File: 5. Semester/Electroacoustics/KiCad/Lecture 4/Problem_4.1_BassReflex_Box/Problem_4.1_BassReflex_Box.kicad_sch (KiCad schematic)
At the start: 14 parts

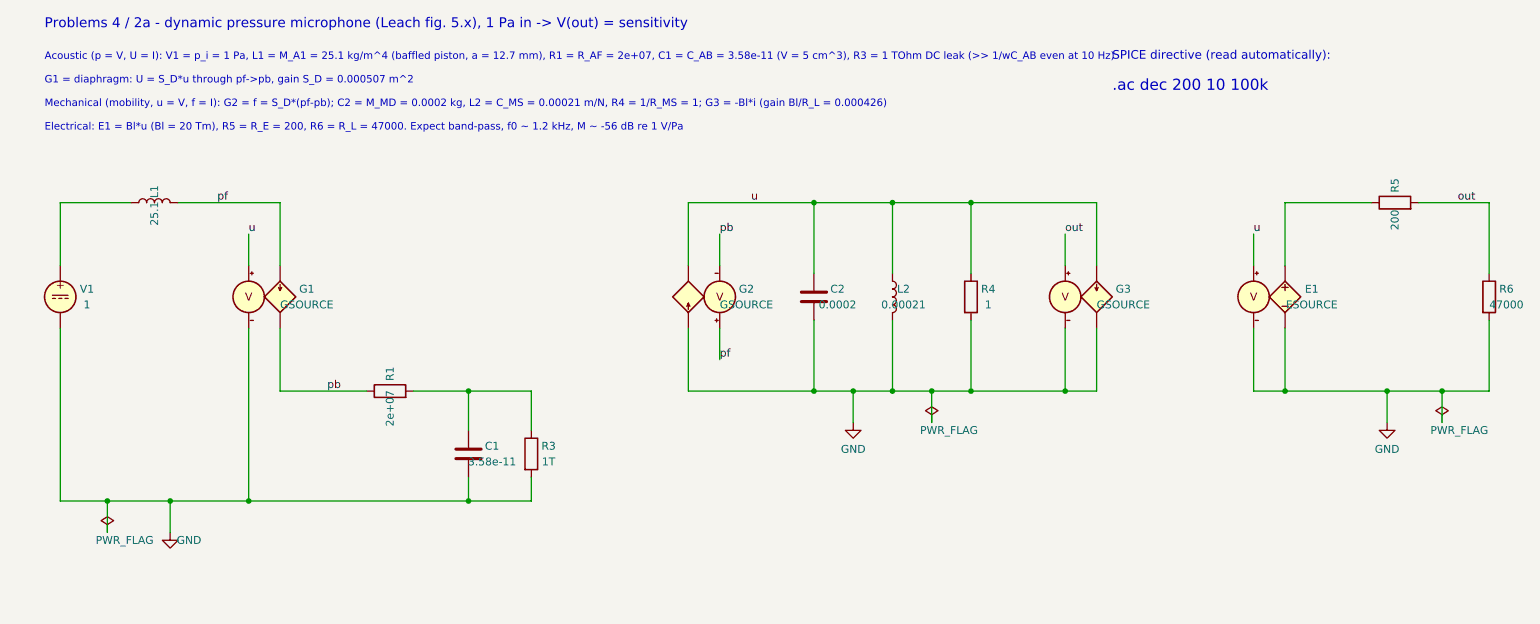
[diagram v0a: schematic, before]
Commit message: Work through the Lecture 4 problems and the Problems 4 mic sheet, reorganize the KiCad sims
- New KiCad/ngspice projects: massless piston (4A slide 9), bass reflex box
  (4.1), piston+baffle+box in both analogies (4.2/4.4a), the designed mic
  (sheet problem 1), and the back-network experiments (sheet 2b-d)
- Sort KiCad projects into Lecture 3 / Lecture 4 / Problems 4 subfolders,
  fix helper imports and template paths, add a README
- Lecture 4 note: plain-language pop-quiz section, tikz circuits for 1a/4.1a/2a,
  sim results and plots throughout, slide anchors on the section headers,
  correct the 4B section's made-up slide references (the handout is 7 slides;
  4c-4d are Leach 5.4 / the problem sheet)
- Obsidian: enable hypersketch plugin, add sketch assets
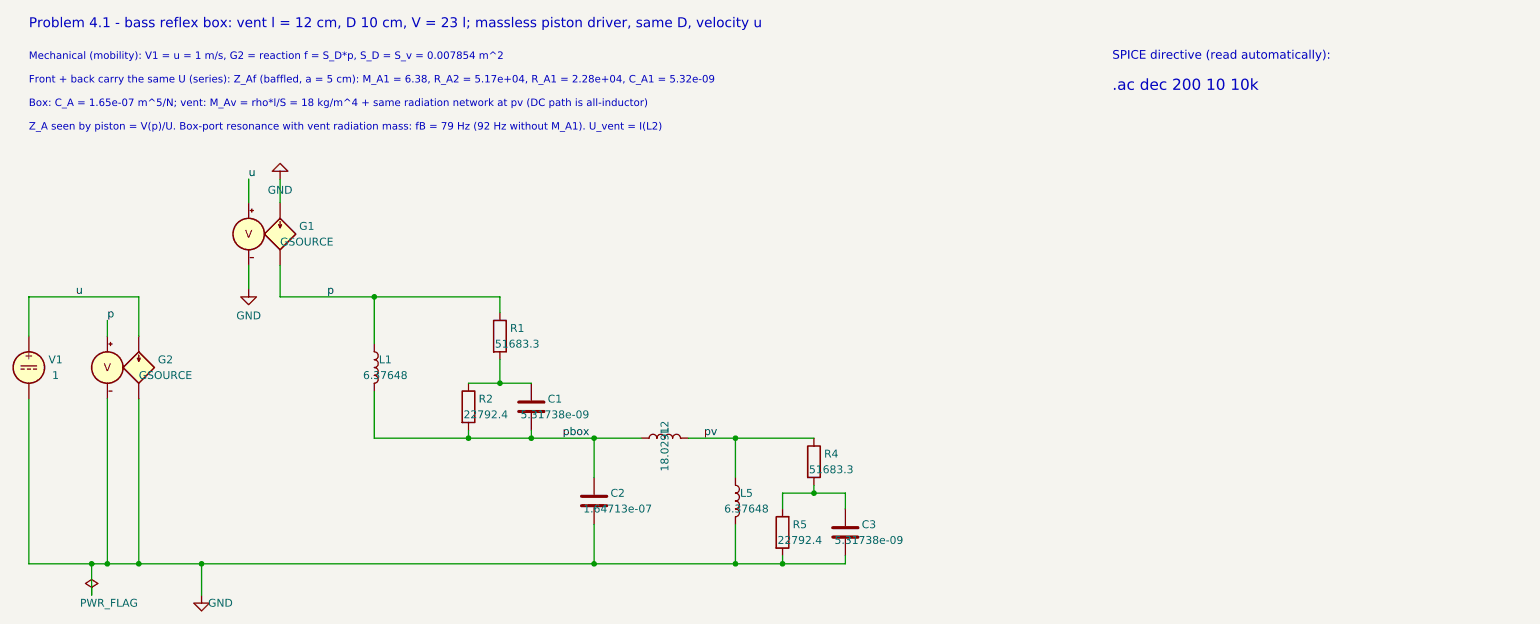
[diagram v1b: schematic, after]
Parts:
- removed E1: ESOURCE, symbol Simulation_SPICE:ESOURCE
- removed G3: GSOURCE, symbol Simulation_SPICE:GSOURCE
- removed R3: 1T, symbol Device:R
- removed R6: 47000, symbol Device:R
- added C3: 5.31738e-09, symbol Device:C
- added L5: 6.37648, symbol Device:L
- added R2: 22792.4, symbol Device:R
- C1: value 3.58e-11 -> 5.31738e-09
- C2: value 0.0002 -> 1.64713e-07
- L1: value 25.1 -> 6.37648
- L2: value 0.00021 -> 18.0291
- R1: value 2e+07 -> 51683.3
- R4: value 1 -> 51683.3
- R5: value 200 -> 22792.4
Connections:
- net out is gone; now on net GND: R5.2
- net GND: now also G1.1 (N+), G2.2 (N-), G2.4 (C-), C3.2, L5.2; no longer C1.2, G2.1 (N+), L2.2, R4.2
- net u: now also G2.1 (N+), V1.1; no longer C2.1, G2.2 (N-), L2.1, R4.1
- net at C1.1, R1.2: now also R2.1
- net p: now reaches L1.1
- net p: now also G1.2 (N-), G2.3 (C+), R1.1; no longer V1.1
- net at R5.1: now also R4.2, C3.1
- removed net pb: G1.2 (N-), G2.4 (C-), R1.1
- removed net pf: G1.1 (N+), G2.3 (C+), L1.2
- new net pbox: C1.2, C2.1, L1.2, L2.1, R2.2
- new net pv: L2.2, L5.1, R4.1
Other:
- note added: ".ac dec 200 10 10k"
- note added: "Box: C_A = 1.65e-07 m^5/N; vent: M_Av = rho*l/S = 18 kg/m^4 + same radiation network at pv (DC path is all-inductor)"
- note added: "Front + back carry the same U (series): Z_Af (baffled, a = 5 cm): M_A1 = 6.38, R_A2 = 5.17e+04, R_A1 = 2.28e+04, C_A1 = 5.32e-09"
- note added: "Mechanical (mobility): V1 = u = 1 m/s, G2 = reaction f = S_D*p, S_D = S_v = 0.007854 m^2"
- note added: "Problem 4.1 - bass reflex box: vent l = 12 cm, D 10 cm, V = 23 l; massless piston driver, same D, velocity u"
- note added: "Z_A seen by piston = V(p)/U. Box-port resonance with vent radiation mass: fB = 79 Hz (92 Hz without M_A1). U_vent = I(L2)"
- note removed: ".ac dec 200 10 100k"
- note removed: "Acoustic (p = V, U = I): V1 = p_i = 1 Pa, L1 = M_A1 = 25.1 kg/m^4 (baffled piston, a = 12.7 mm), R1 = R_AF = 2e+07, C1 = C_AB = 3.58e-11 (V = 5 cm^3), R3 = 1 TOhm DC leak (>> 1/wC_AB even at 10 Hz)"
- note removed: "Electrical: E1 = Bl*u (Bl = 20 Tm), R5 = R_E = 200, R6 = R_L = 47000. Expect band-pass, f0 ~ 1.2 kHz, M ~ -56 dB re 1 V/Pa"
- note removed: "G1 = diaphragm: U = S_D*u through pf->pb, gain S_D = 0.000507 m^2"
- note removed: "Mechanical (mobility, u = V, f = I): G2 = f = S_D*(pf-pb); C2 = M_MD = 0.0002 kg, L2 = C_MS = 0.00021 m/N, R4 = 1/R_MS = 1; G3 = -Bl*i (gain Bl/R_L = 0.000426)"
- note removed: "Problems 4 / 2a - dynamic pressure microphone (Leach fig. 5.x), 1 Pa in -> V(out) = sensitivity"
- title: Problems 4 (2a) - Dynamic pressure microphone, three domains -> Problem 4.1 - bass reflex box, Z_A and far field
